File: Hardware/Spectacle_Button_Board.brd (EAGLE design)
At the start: 44.5 x 73.7 mm, 54 parts, among them J17 AUDIO-JACK3, J20 AUDIO-JACK3, U1 CY8C4146LQI-S422, U2 3.3V/150mA, U4 SN74LVC1G66, U5 SN74LVC1G66

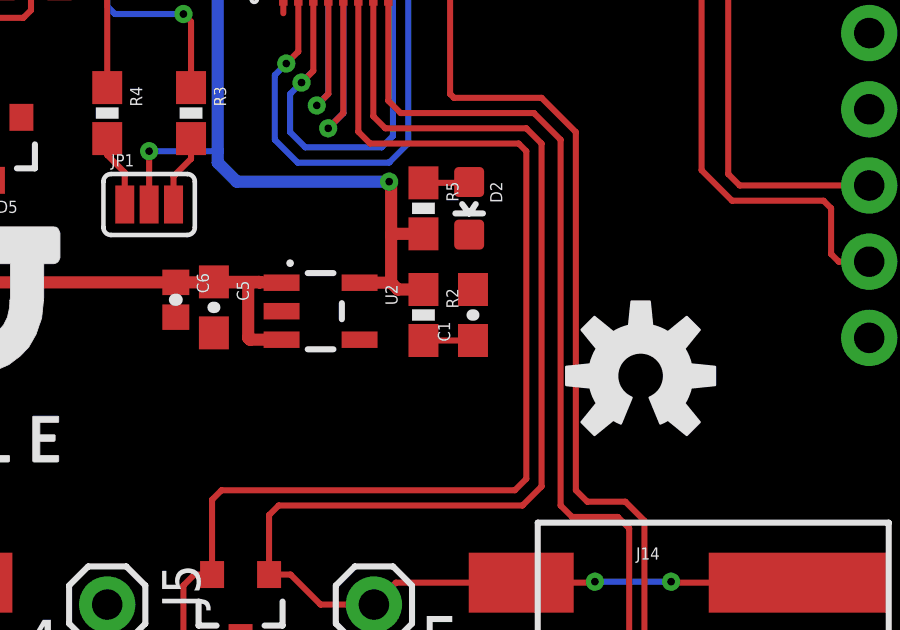
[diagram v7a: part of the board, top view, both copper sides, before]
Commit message: Chg VREG to APK2112
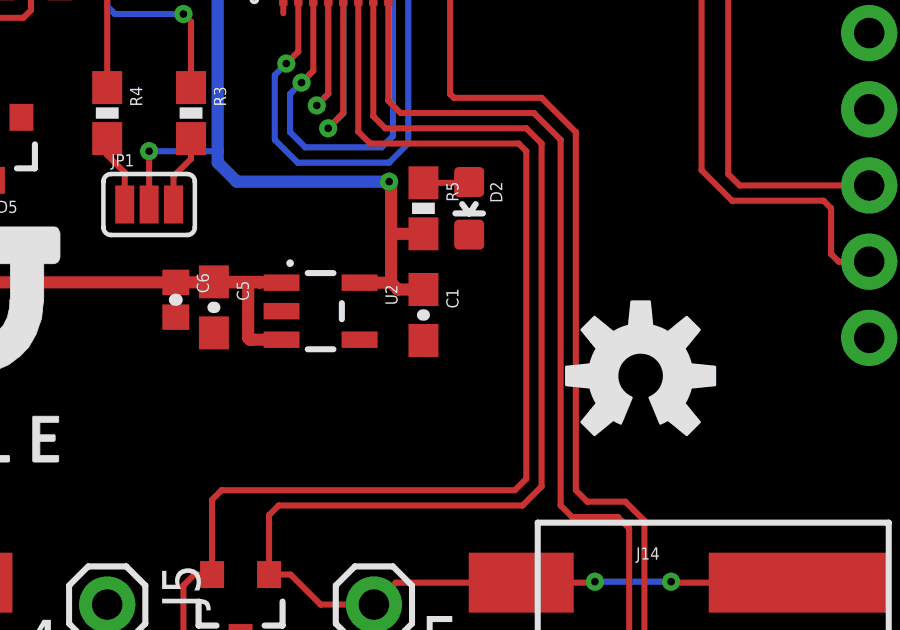
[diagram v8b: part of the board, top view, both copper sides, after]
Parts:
- removed R2: 0.27, SparkFun-Resistors:0603-RES
- U2: value 3.3V/150mA -> 3.3V
- moved C1 1.65 mm to (28.3, 24.9), turned to 270 degrees
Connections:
- removed net N$3: C1.1, R2.2
- net 3.3V: now also C1.1; no longer R2.1
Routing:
- net N$3: track 1.65 -> 0.00 mm
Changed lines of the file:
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@@
 <layers>
 <layer number="1" name="Top" color="4" fill="1" visible="yes" active="yes"/>
-<layer number="2" name="Route2" color="1" fill="3" visible="yes" active="yes"/>
-<layer number="15" name="Route15" color="4" fill="6" visible="yes" active="yes"/>
+<layer number="2" name="Route2" color="1" fill="3" visible="no" active="yes"/>
+<layer number="15" name="Route15" color="4" fill="6" visible="no" active="yes"/>
 <layer number="16" name="Bottom" color="1" fill="1" visible="yes" active="yes"/>
 <layer number="17" name="Pads" color="2" fill="1" visible="yes" active="yes"/>
@@
 <layer number="23" name="tOrigins" color="15" fill="1" visible="yes" active="yes"/>
 <layer number="24" name="bOrigins" color="15" fill="1" visible="yes" active="yes"/>
-<layer number="25" name="tNames" color="7" fill="1" visible="yes" active="yes"/>
-<layer number="26" name="bNames" color="7" fill="1" visible="yes" active="yes"/>
-<layer number="27" name="tValues" color="7" fill="1" visible="yes" active="yes"/>
-<layer number="28" name="bValues" color="7" fill="1" visible="yes" active="yes"/>
-<layer number="29" name="tStop" color="7" fill="3" visible="yes" active="yes"/>
-<layer number="30" name="bStop" color="7" fill="6" visible="yes" active="yes"/>
-<layer number="31" name="tCream" color="7" fill="4" visible="yes" active="yes"/>
-<layer number="32" name="bCream" color="7" fill="5" visible="yes" active="yes"/>
-<layer number="39" name="tKeepout" color="4" fill="11" visible="yes" active="yes"/>
-<layer number="40" name="bKeepout" color="1" fill="11" visible="yes" active="yes"/>
-<layer number="41" name="tRestrict" color="4" fill="10" visible="yes" active="yes"/>
-<layer number="42" name="bRestrict" color="1" fill="10" visible="yes" active="yes"/>
-<layer number="43" name="vRestrict" color="2" fill="10" visible="yes" active="yes"/>
-<layer number="44" name="Drills" color="7" fill="1" visible="yes" active="yes"/>
+<layer number="25" name="tNames" color="7" fill="1" visible="no" active="yes"/>
+<layer number="26" name="bNames" color="7" fill="1" visible="no" active="yes"/>
+<layer number="27" name="tValues" color="7" fill="1" visible="no" active="yes"/>
+<layer number="28" name="bValues" color="7" fill="1" visible="no" active="yes"/>
+<layer number="29" name="tStop" color="7" fill="3" visible="no" active="yes"/>
+<layer number="30" name="bStop" color="7" fill="6" visible="no" active="yes"/>
+<layer number="31" name="tCream" color="7" fill="4" visible="no" active="yes"/>
+<layer number="32" name="bCream" color="7" fill="5" visible="no" active="yes"/>
+<layer number="39" name="tKeepout" color="4" fill="11" visible="no" active="yes"/>
+<layer number="40" name="bKeepout" color="1" fill="11" visible="no" active="yes"/>
+<layer number="41" name="tRestrict" color="4" fill="10" visible="no" active="yes"/>
+<layer number="42" name="bRestrict" color="1" fill="10" visible="no" active="yes"/>
+<layer number="43" name="vRestrict" color="2" fill="10" visible="no" active="yes"/>
+<layer number="44" name="Drills" color="7" fill="1" visible="no" active="yes"/>
 <layer number="45" name="Holes" color="7" fill="1" visible="yes" active="yes"/>
-<layer number="46" name="Milling" color="3" fill="1" visible="yes" active="yes"/>
-<layer number="47" name="Measures" color="7" fill="1" visible="yes" active="yes"/>
-<layer number="48" name="Document" color="7" fill="1" visible="yes" active="yes"/>
-<layer number="49" name="Reference" color="7" fill="1" visible="yes" active="yes"/>
+<layer number="46" name="Milling" color="3" fill="1" visible="no" active="yes"/>
+<layer number="47" name="Measures" color="7" fill="1" visible="no" active="yes"/>
+<layer number="48" name="Document" color="7" fill="1" visible="no" active="yes"/>
+<layer number="49" name="Reference" color="7" fill="1" visible="no" active="yes"/>
 <layer number="51" name="tDocu" color="6" fill="1" visible="yes" active="yes"/>
-<layer number="52" name="bDocu" color="7" fill="1" visible="yes" active="yes"/>
+<layer number="52" name="bDocu" color="7" fill="1" visible="no" active="yes"/>
 <layer number="3" name="Route3" color="4" fill="3" visible="no" active="no"/>
 <layer number="4" name="Route4" color="1" fill="4" visible="no" active="no"/>
@@
 <attribute name="PROD_ID" value="IC-13286" x="25.4" y="38.1" size="1.778" layer="27" display="off"/>
 </element>
-<element name="U2" library="SparkFun-PowerIC" package="SOT23-5" value="3.3V/150mA" x="24.892" y="25.019" rot="R270">
-<attribute name="PROD_ID" value="VREG-00822" x="24.892" y="25.019" size="1.778" layer="27" font="vector" ratio="15" rot="R270" display="off"/>
+<element name="U2" library="SparkFun-PowerIC" package="SOT23-5" value="3.3V" x="24.892" y="25.019" rot="R270">
+<attribute name="PROD_ID" value="VREG-12457" x="24.892" y="25.019" size="1.778" layer="27" font="vector" ratio="15" rot="R270" display="off"/>
 </element>
 <element name="J1" library="SparkFun-Connectors" package="1X02" value="" x="17.78" y="69.85" rot="R270"/>
@@
 <attribute name="PROD_ID" value="RES-00824" x="22.225" y="43.434" size="1.778" layer="27" font="vector" ratio="15" rot="R180" display="off"/>
 </element>
-<element name="R2" library="SparkFun-Resistors" package="0603-RES" value="0.27" x="28.321" y="24.892" rot="R270">
-<attribute name="PROD_ID" value="RES-08787" x="28.321" y="24.892" size="1.778" layer="27" font="vector" ratio="15" rot="R270" display="off"/>
-</element>
-<element name="C1" library="SparkFun-Capacitors" package="0603-CAP" value="2.2uF" x="29.972" y="24.892" rot="R90">
-<attribute name="PROD_ID" value="CAP-07888" x="29.972" y="24.892" size="1.778" layer="27" font="vector" ratio="15" rot="R90" display="off"/>
+<element name="C1" library="SparkFun-Capacitors" package="0603-CAP" value="2.2uF" x="28.321" y="24.892" rot="R270">
+<attribute name="PROD_ID" value="CAP-07888" x="28.321" y="24.892" size="1.778" layer="27" font="vector" ratio="15" rot="R270" display="off"/>
 </element>
 <element name="C2" library="SparkFun-Capacitors" package="0402-CAP" value="1.0uF" x="19.939" y="37.465" rot="R180">
@@
 <wire x1="24.511" y1="45.72" x2="23.965" y2="45.174" width="0.2032" layer="1"/>
 <wire x1="23.132" y1="45.174" x2="23.965" y2="45.174" width="0.2032" layer="1"/>
-</signal>
-<signal name="N$3">
-<contactref element="R2" pad="2"/>
-<contactref element="C1" pad="1"/>
-<wire x1="28.321" y1="24.042" x2="29.972" y2="24.042" width="0.2032" layer="1"/>
 </signal>
 <signal name="VIN">
@@
 <contactref element="C3" pad="1"/>
 <contactref element="U2" pad="5"/>
-<contactref element="R2" pad="1"/>
 <contactref element="J18" pad="1"/>
 <contactref element="JP1" pad="2"/>
@@
 <wire x1="21.959" y1="38.85" x2="21.844" y2="38.735" width="0.2032" layer="1"/>
 <wire x1="26.1921" y1="25.969" x2="27.244" y2="25.969" width="0.4064" layer="1"/>
-<wire x1="28.321" y1="25.742" x2="27.471" y2="25.742" width="0.4064" layer="1"/>
 <wire x1="27.471" y1="25.742" x2="27.244" y2="25.969" width="0.4064" layer="1"/>
 <wire x1="28.321" y1="27.598" x2="27.283" y2="27.598" width="0.4064" layer="1"/>
@@
 <via x="19.177" y="30.353" extent="1-16" drill="0.254"/>
 <wire x1="19.177" y1="30.353" x2="21.463" y2="30.353" width="0.2032" layer="16"/>
+<contactref element="C1" pad="1"/>
+<wire x1="28.321" y1="25.742" x2="27.471" y2="25.742" width="0.4064" layer="1"/>
 </signal>
 <signal name="I2C_OUT_EN">
